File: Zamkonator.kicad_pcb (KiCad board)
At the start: 2 copper layers, 75 x 75 mm, 143 parts, among them J1 Screw_Terminal_01x06, J2 Micro_SD_Card_Det1, J3 Conn_01x08_Male, J4 Screw_Terminal_01x06, J5 Conn_01x04_Female, J6 Conn_01x03_Female, K1 SRD-DC3V-SL-C, Q1 DMG2302U, T1 HR051142, U1 RTL8201F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

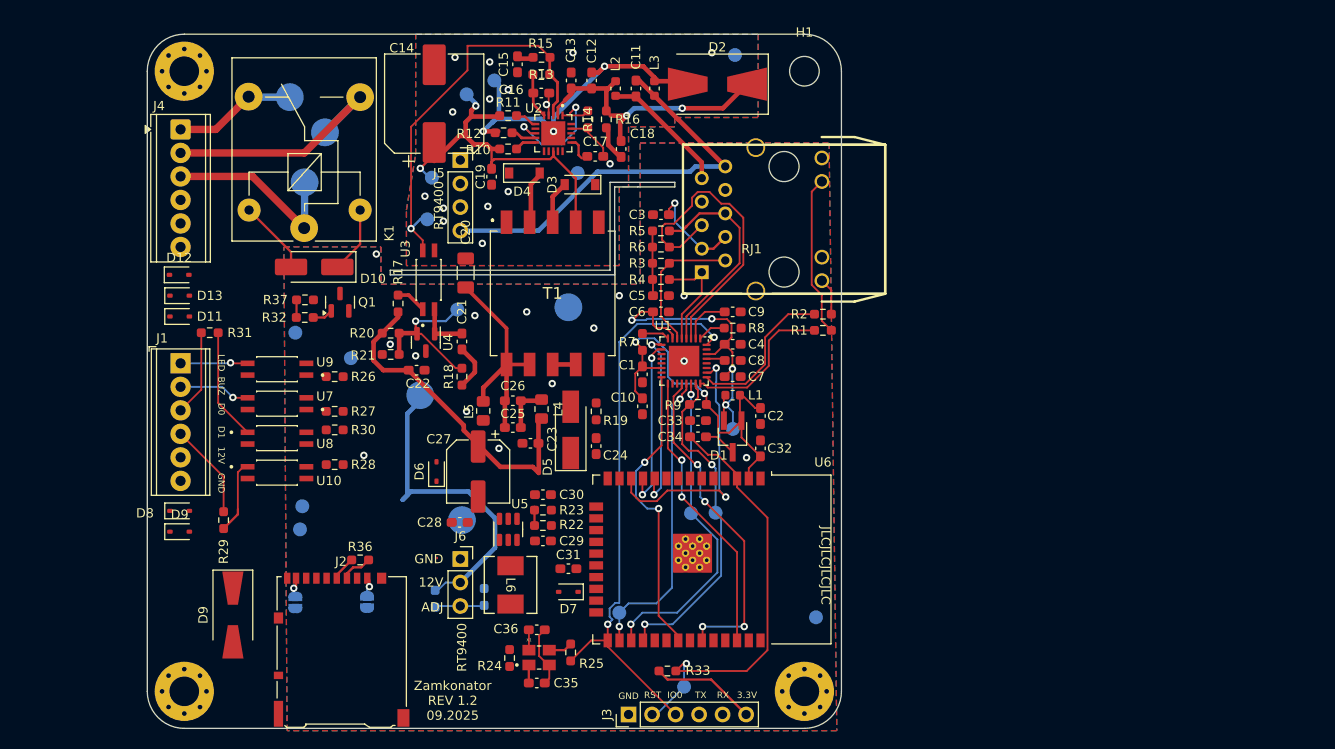
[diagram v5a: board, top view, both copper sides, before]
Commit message: Remove custom library for EL3H7, use the kicad one.
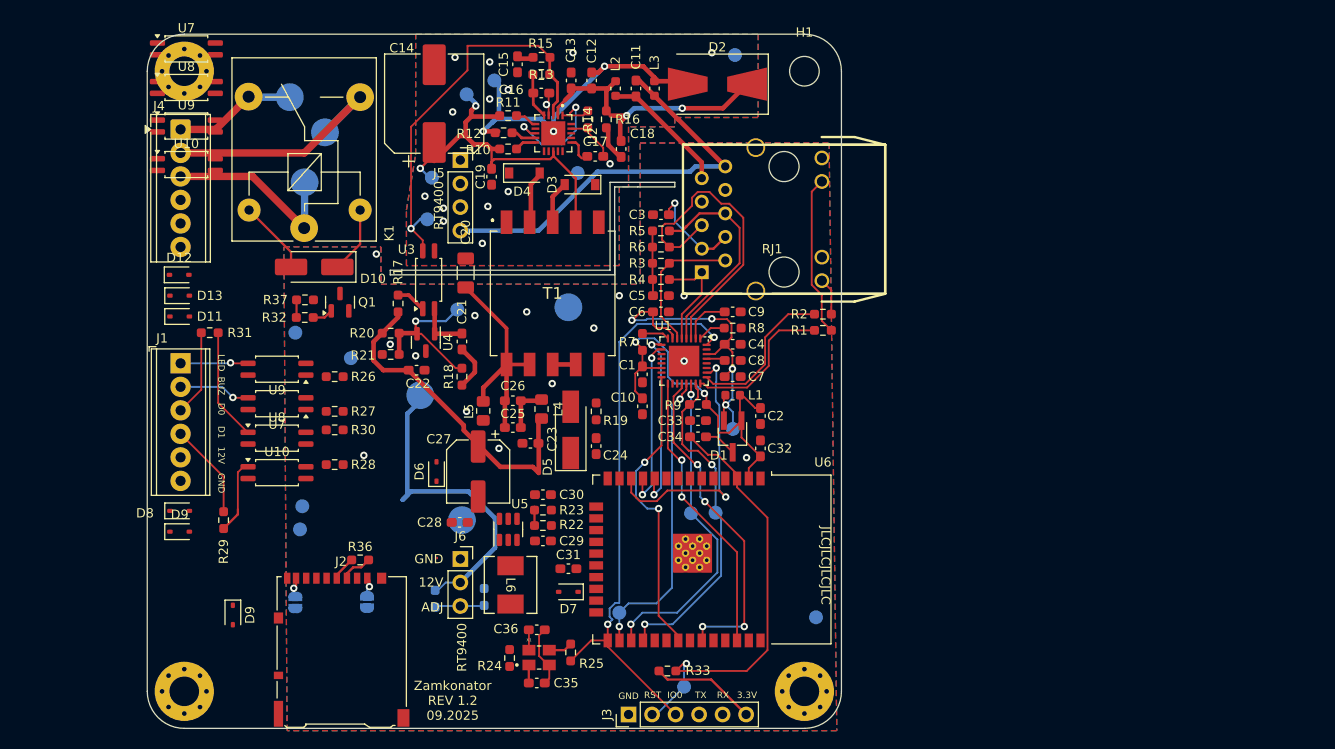
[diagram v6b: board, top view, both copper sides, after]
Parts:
- added U10: EL3H7-G, Package_SO:SSOP-4_4.4x2.6mm_P1.27mm, F.Cu at (4.22, 14.1)
- added U7: EL3H7-G, Package_SO:SSOP-4_4.4x2.6mm_P1.27mm, F.Cu at (4.22, 1.59)
- added U8: EL3H7-G, Package_SO:SSOP-4_4.4x2.6mm_P1.27mm, F.Cu at (4.22, 5.75)
- added U9: EL3H7-G, Package_SO:SSOP-4_4.4x2.6mm_P1.27mm, F.Cu at (4.22, 9.92)
- D9: value 5V5 -> PESD5V0L1BA; footprint Diode_SMD:D_SMA-SMB_Universal_Handsoldering -> Diode_SMD:D_SOD-323
- L6: footprint panasonic_coil:IND_PCC-M0530M-LP_PAN -> project_footprints:IND_PCC-M0530M-LP_PAN
- RJ1: footprint project specific:RJ45-TH_HY931147C -> project_footprints:RJ45-TH_HY931147C
- T1: footprint project specific:HR051142 -> project_footprints:HR051142
- U10, U3, U7, U8, U9: footprint project specific:SOIC127P700X200-4N -> Package_SO:SSOP-4_4.4x2.6mm_P1.27mm
- U2: footprint project specific:QFN50P400X400X90-21N -> project_footprints:QFN50P400X400X90-21N
- X1: footprint project specific:XTAL_TSX-3225_16.0000MF18X-AC3 -> project_footprints:XTAL_TSX-3225_16.0000MF18X-AC3
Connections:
- D9 pad 1: Net-(D9-A1) -> GND2
- D9 pad 2: GND2 -> Net-(D9-A2)
- U10 pad 1: Net-(D8-A2) -> /DAT1_INV
- U10 pad 2: GND2 -> GND
- U10 pad 3: GND -> GND2
- U10 pad 4: /DAT1_INV -> Net-(D8-A2)
- U8 pad 1: Net-(D9-A2) -> /DAT0_INV
- U8 pad 2: GND2 -> GND
- U8 pad 3: GND -> GND2
- U8 pad 4: /DAT0_INV -> Net-(D9-A2)

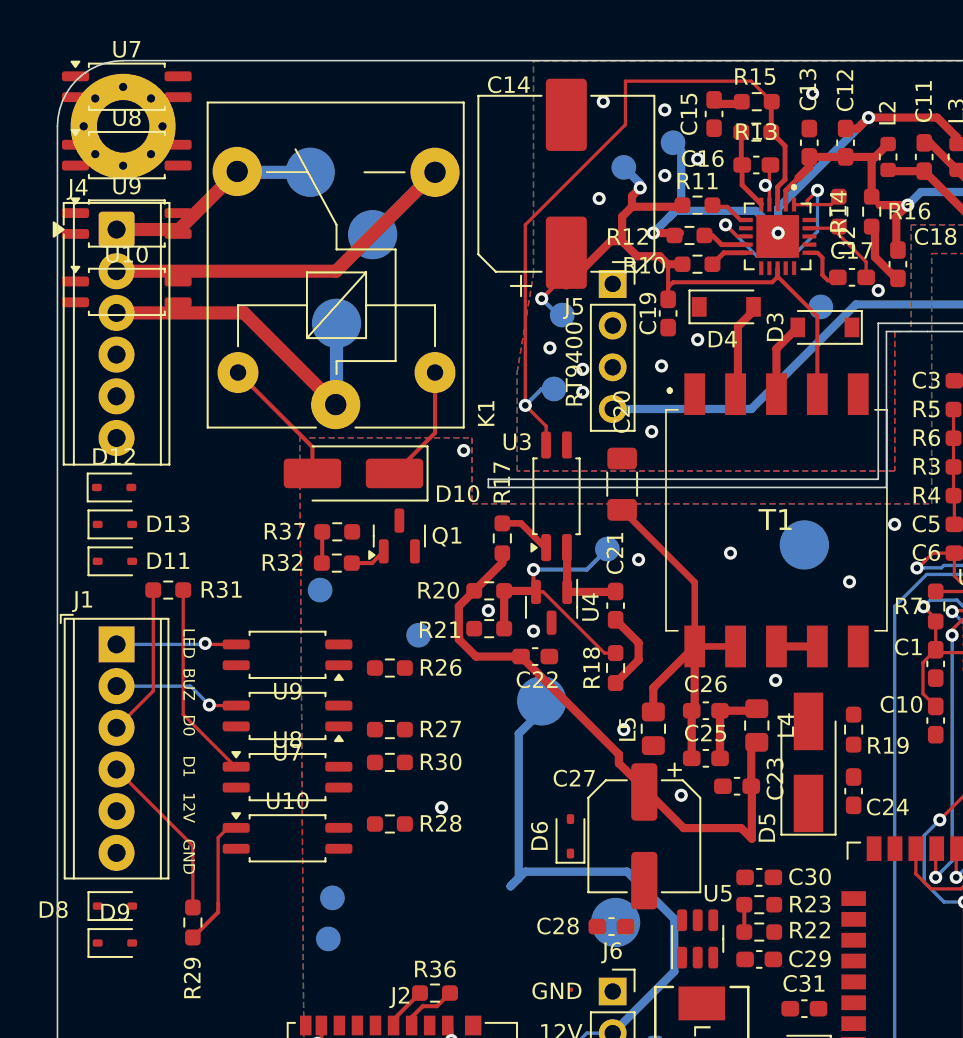
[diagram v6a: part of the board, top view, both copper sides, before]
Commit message: remove custom footprint for Si3404
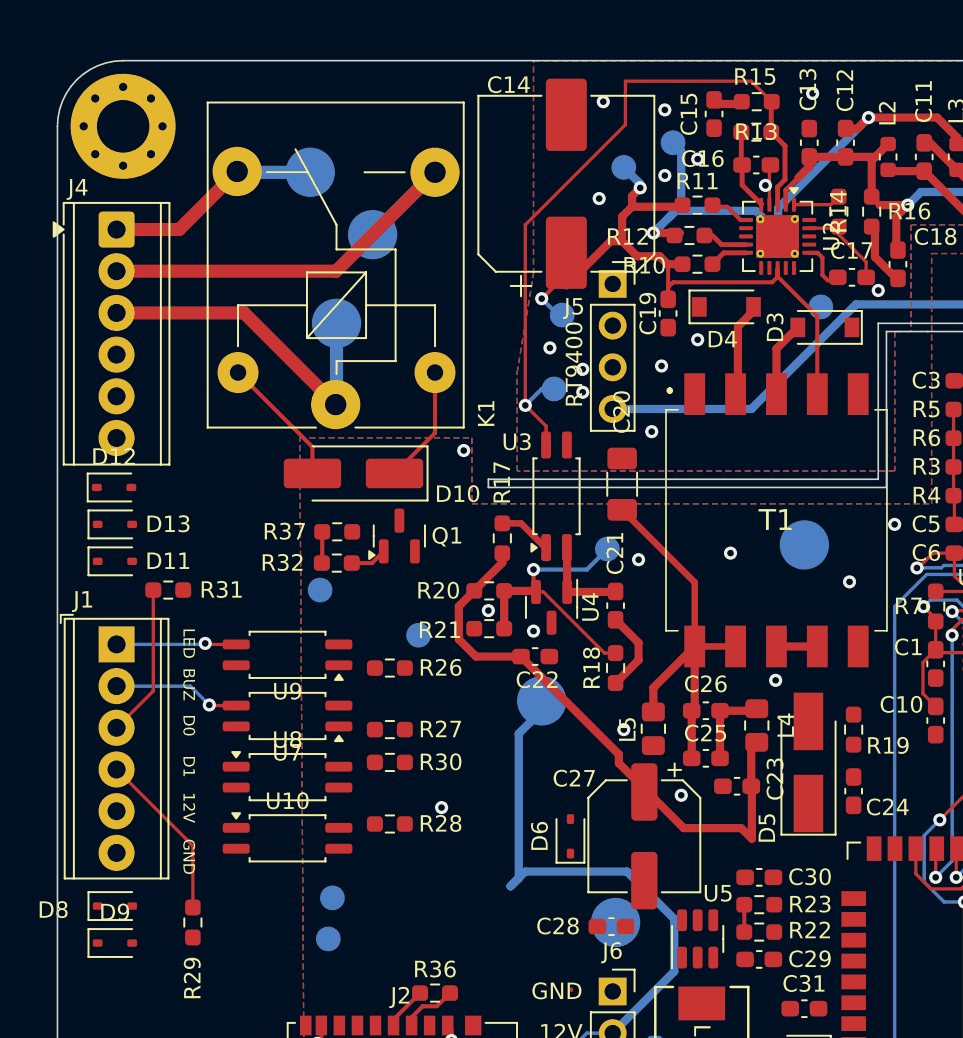
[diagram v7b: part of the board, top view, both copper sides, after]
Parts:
- removed the U10 at (4.22, 14.1)
- removed the U7 at (4.22, 1.59)
- removed the U8 at (4.22, 5.75)
- removed the U9 at (4.22, 9.92)
- U2: footprint project_footprints:QFN50P400X400X90-21N -> Package_DFN_QFN:MLF-20-1EP_4x4mm_P0.5mm_EP2.6x2.6mm_ThermalVias
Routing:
- net Net-(U2-HSO): track 15.1 -> 2.93 mm, vias 2 -> 0
- net Net-(D9-A2): track 12.1 -> 0.00 mm
- net Net-(D8-A2): track 8.01 -> 0.00 mm
- net Net-(D2-A): vias 3 -> 2

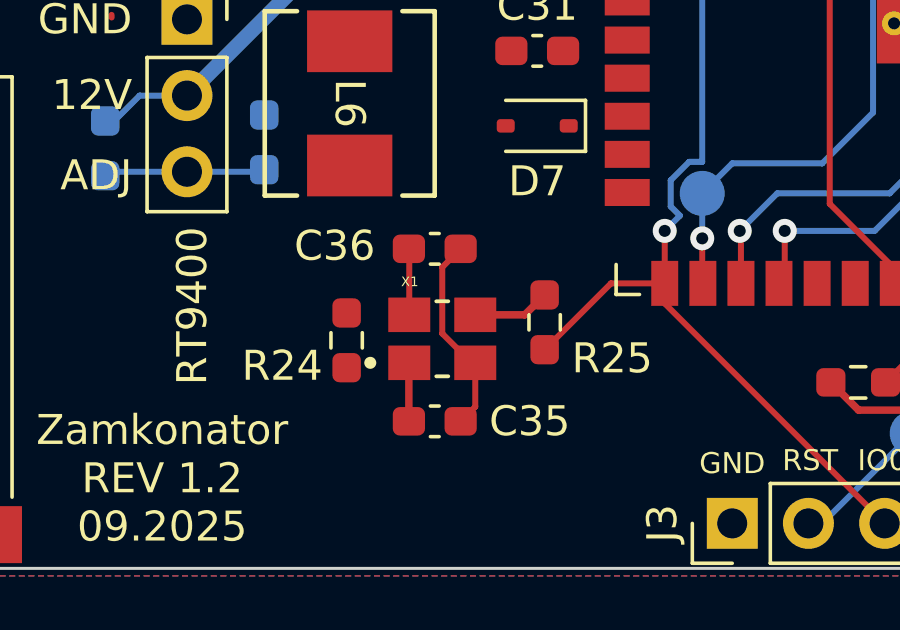
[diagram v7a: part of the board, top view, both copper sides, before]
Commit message: Update crystal LCSC number, use built-in footprint
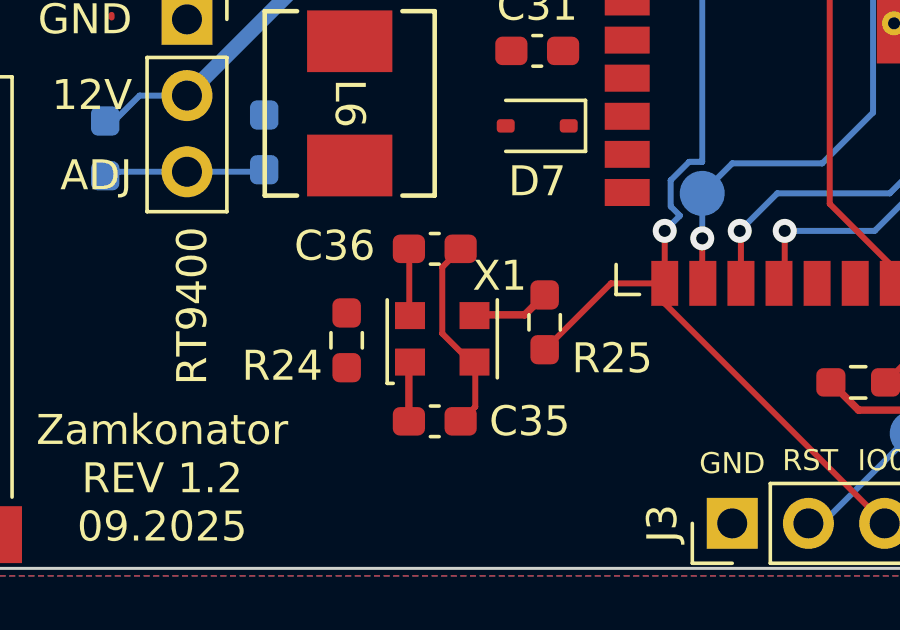
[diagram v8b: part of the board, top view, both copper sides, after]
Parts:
- X1: value S3D50.000000B20F30T -> SX3M50.000M20F30TNN; footprint project_footprints:XTAL_TSX-3225_16.0000MF18X-AC3 -> Oscillator:Oscillator_SMD_EuroQuartz_XO32-4Pin_3.2x2.5mm
- turned X1 to 90 degrees
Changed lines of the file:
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@@
 		)
 	)
-	(footprint "project_footprints:XTAL_TSX-3225_16.0000MF18X-AC3"
+	(footprint "Oscillator:Oscillator_SMD_EuroQuartz_XO32-4Pin_3.2x2.5mm"
 		(layer "F.Cu")
-		(at 42.335 67.348)
+		(at 42.335 67.348 90)
+		(descr "Miniature Crystal Clock Oscillator EuroQuartz XO32 series, http://cdn-reichelt.de/documents/datenblatt/B400/XO32.pdf, 3.2x2.5mm^2 package")
+		(tags "SMD SMT crystal oscillator")
 		(property "Reference" "X1"
-			(at -1.084 -1.9032 0)
+			(at 2.098 1.915 180)
 			(layer "F.SilkS")
 			(effects
 				(font
-					(size 0.32 0.32)
-					(thickness 0.15)
-				)
-			)
-		)
-		(property "Value" "S3D50.000000B20F30T"
-			(at 3.996 1.8968 0)
-			(layer "F.Fab")
-			(effects
-				(font
-					(size 0.32 0.32)
-					(thickness 0.15)
-				)
-			)
-		)
-		(property "Datasheet" "https://www.lcsc.com/datasheet/lcsc_datasheet_2209071730_Shenzhen-SCTF-Elec-S3D50-000000B20F30T_C387445.pdf"
-			(at 0 0 0)
+					(size 1 1)
+					(thickness 0.15)
+				)
+			)
+		)
+		(property "Value" "SX3M50.000M20F30TNN"
+			(at 0 2.45 90)
+			(layer "F.Fab")
+			(effects
+				(font
+					(size 1 1)
+					(thickness 0.15)
+				)
+			)
+		)
+		(property "Datasheet" "https://www.lcsc.com/datasheet/C2901592.pdf"
+			(at 0 0 90)
+			(unlocked yes)
 			(layer "F.Fab")
 			(hide yes)
@@
 		)
 		(property "Description" ""
-			(at 0 0 0)
+			(at 0 0 90)
+			(unlocked yes)
 			(layer "F.Fab")
 			(hide yes)
@@
 			)
 		)
-		(property "LCSC" "C387445"
-			(at 0 0 0)
+		(property "LCSC" "C2901592"
+			(at 0 0 90)
 			(unlocked yes)
 			(layer "F.Fab")
@@
 		(sheetname "/50MHZ CLOCK/")
 		(sheetfile "CLOCK.kicad_sch")
-		(attr through_hole)
-		(fp_line
-			(start -0.2 -1.25)
-			(end 0.2 -1.25)
-			(stroke
-				(width 0.127)
+		(attr smd)
+		(fp_line
+			(start -1.485 -1.835)
+			(end 1.3 -1.835)
+			(stroke
+				(width 0.12)
 				(type solid)
 			)
@@
 		)
 		(fp_line
-			(start -0.2 1.25)
-			(end 0.2 1.25)
-			(stroke
-				(width 0.127)
+			(start -1.485 -1.635)
+			(end -1.485 -1.835)
+			(stroke
+				(width 0.12)
 				(type solid)
 			)
 			(layer "F.SilkS")
 		)
+		(fp_line
+			(start 1.3 1.835)
+			(end -1.3 1.835)
+			(stroke
+				(width 0.12)
+				(type solid)
+			)
+			(layer "F.SilkS")
+		)
 		(fp_circle
-			(center -2.4 0.8)
-			(end -2.3 0.8)
-			(stroke
-				(width 0.2)
+			(center 0 0)
+			(end 0 0.058333)
+			(stroke
+				(width 0.116667)
 				(type solid)
 			)
 			(fill no)
-			(layer "F.SilkS")
-		)
-		(fp_line
-			(start -2.05 -1.62)
-			(end 2.05 -1.62)
+			(layer "F.Adhes")
+		)
+		(fp_circle
+			(center 0 0)
+			(end 0 0.133333)
+			(stroke
+				(width 0.083333)
+				(type solid)
+			)
+			(fill no)
+			(layer "F.Adhes")
+		)
+		(fp_circle
+			(center 0 0)
+			(end 0 0.208333)
+			(stroke
+				(width 0.083333)
+				(type solid)
+			)
+			(fill no)
+			(layer "F.Adhes")
+		)
+		(fp_circle
+			(center 0 0)
+			(end 0 0.25)
+			(stroke
+				(width 0.1)
+				(type solid)
+			)
+			(fill no)
+			(layer "F.Adhes")
+		)
+		(fp_line
+			(start 1.5 -1.9)
+			(end -1.5 -1.9)
 			(stroke
 				(width 0.05)
@@
 		)
 		(fp_line
-			(start -2.05 1.62)
-			(end -2.05 -1.62)
+			(start -1.5 -1.9)
+			(end -1.5 1.9)
 			(stroke
 				(width 0.05)
@@
 		)
 		(fp_line
-			(start 2.05 -1.62)
-			(end 2.05 1.62)
+			(start 1.5 1.9)
+			(end 1.5 -1.9)
 			(stroke
 				(width 0.05)
@@
 		)
 		(fp_line
-			(start 2.05 1.62)
-			(end -2.05 1.62)
+			(start -1.5 1.9)
+			(end 1.5 1.9)
 			(stroke
 				(width 0.05)
@@
 		)
 		(fp_line
-			(start -1.6 -1.25)
-			(end 1.6 -1.25)
-			(stroke
-				(width 0.127)
-				(type solid)
-			)
-			(layer "F.Fab")
-		)
-		(fp_line
-			(start -1.6 1.25)
-			(end -1.6 -1.25)
-			(stroke
-				(width 0.127)
-				(type solid)
-			)
-			(layer "F.Fab")
-		)
-		(fp_line
-			(start 1.6 -1.25)
-			(end 1.6 1.25)
-			(stroke
-				(width 0.127)
-				(type solid)
-			)
-			(layer "F.Fab")
-		)
-		(fp_line
-			(start 1.6 1.25)
-			(end -1.6 1.25)
-			(stroke
-				(width 0.127)
-				(type solid)
-			)
-			(layer "F.Fab")
-		)
-		(fp_circle
-			(center -2.4 0.8)
-			(end -2.3 0.8)
-			(stroke
-				(width 0.2)
-				(type solid)
-			)
-			(fill no)
-			(layer "F.Fab")
+			(start 1.15 -1.6)
+			(end 1.25 -1.5)
+			(stroke
+				(width 0.1)
+				(type solid)
+			)
+			(layer "F.Fab")
+		)
+		(fp_line
+			(start -0.25 -1.6)
+			(end -1.25 -0.6)
+			(stroke
+				(width 0.1)
+				(type solid)
+			)
+			(layer "F.Fab")
+		)
+		(fp_line
+			(start -1.15 -1.6)
+			(end 1.15 -1.6)
+			(stroke
+				(width 0.1)
+				(type solid)
+			)
+			(layer "F.Fab")
+		)
+		(fp_line
+			(start 1.25 -1.5)
+			(end 1.25 1.5)
+			(stroke
+				(width 0.1)
+				(type solid)
+			)
+			(layer "F.Fab")
+		)
+		(fp_line
+			(start -1.25 -1.5)
+			(end -1.15 -1.6)
+			(stroke
+				(width 0.1)
+				(type solid)
+			)
+			(layer "F.Fab")
+		)
+		(fp_line
+			(start 1.25 1.5)
+			(end 1.15 1.6)
+			(stroke
+				(width 0.1)
+				(type solid)
+			)
+			(layer "F.Fab")
+		)
+		(fp_line
+			(start -1.25 1.5)
+			(end -1.25 -1.5)
+			(stroke
+				(width 0.1)
+				(type solid)
+			)
+			(layer "F.Fab")
+		)
+		(fp_line
+			(start 1.15 1.6)
+			(end -1.15 1.6)
+			(stroke
+				(width 0.1)
+				(type solid)
+			)
+			(layer "F.Fab")
+		)
+		(fp_line
+			(start -1.15 1.6)
+			(end -1.25 1.5)
+			(stroke
+				(width 0.1)
+				(type solid)
+			)
+			(layer "F.Fab")
+		)
+		(fp_text user "${REFERENCE}"
+			(at 0 0 0)
+			(layer "F.Fab")
+			(effects
+				(font
+					(size 0.7 0.7)
+					(thickness 0.105)
+				)
+			)
 		)
 		(pad "1" smd rect
-			(at -1.1 0.8)
-			(size 1.4 1.15)
+			(at -0.775 -1.075)
+			(size 1 0.9)
 			(layers "F.Cu" "F.Mask" "F.Paste")
 			(net 24 "/CLK_EN")
@@
 		)
 		(pad "2" smd rect
-			(at 1.1 0.8)
-			(size 1.4 1.15)
+			(at -0.775 1.075)
+			(size 1 0.9)
 			(layers "F.Cu" "F.Mask" "F.Paste")
 			(net 1 "GND")
@@
 		)
 		(pad "3" smd rect
-			(at 1.1 -0.8)
-			(size 1.4 1.15)
+			(at 0.775 1.075)
+			(size 1 0.9)
 			(layers "F.Cu" "F.Mask" "F.Paste")
 			(net 64 "Net-(X1-OUT)")
@@
 		)
 		(pad "4" smd rect
-			(at -1.1 -0.8)
-			(size 1.4 1.15)
+			(at 0.775 -1.075)
+			(size 1 0.9)
 			(layers "F.Cu" "F.Mask" "F.Paste")
 			(net 21 "+3.3V")
@@
 		)
 		(embedded_fonts no)
+		(model "${KICAD9_3DMODEL_DIR}/Oscillator.3dshapes/Oscillator_SMD_EuroQuartz_XO32-4Pin_3.2x2.5mm.step"
+			(offset
+				(xyz 0 0 0)
+			)
+			(scale
+				(xyz 1 1 1)
+			)
+			(rotate
+				(xyz 0 0 0)
+			)
+		)
 	)
 	(footprint "Diode_SMD:D_SOD-323"
